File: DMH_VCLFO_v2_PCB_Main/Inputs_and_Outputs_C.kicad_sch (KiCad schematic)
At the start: 41 parts, among them J13 TS_Jack_6.35mm_Sw, J14 TS_Jack_6.35mm_Sw, J15 TS_Jack_6.35mm_Sw, J16 TS_Jack_6.35mm_Sw, J17 TS_Jack_6.35mm_Sw, J18 TS_Jack_6.35mm_Sw, J29 Conn_01x08, J30 Conn_01x08, J31 IDC_02x05, J32 Conn_01x08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

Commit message: Main PCB comp placement in progress
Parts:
- J13: Function CV In A -> CV In C
- J14: Function Sync A -> Sync C
- J15: Function Out A Sqr -> Out C Sqr
- J16: Function Out A Saw -> Out C Saw
- J17: Function Out A Rmp/Rnd -> Out C Rmp/Rnd
- J18: Function Out A Sin/Tri -> Out C Sin/Tri
- J29, J30: footprint Connector_PinHeader_2.54mm:PinHeader_1x08_P2.54mm_Vertical -> Connector_PinSocket_2.54mm:PinSocket_1x08_P2.54mm_Vertical
- RV10: Function Freq A -> Freq C
- RV9: Function CV A Amt -> CV C Amt
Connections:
- net Bus_CV_C: now also J30.5 (Pin_5), SW9.1 (A); no longer J30.8 (Pin_8), SW9.3 (C)
- net Bus_CV_M: now also J33.5 (Pin_5); no longer J33.8 (Pin_8)
- net C_BusCV_Sw_p2_C: now also J30.4 (Pin_4); no longer J30.7 (Pin_7)
- net C_BusCV_Sw_p2_M: now also J33.4 (Pin_4); no longer J33.7 (Pin_7)
- net C_CV_Amt_Pot_p2_C: now also J29.6 (Pin_6); no longer J29.4 (Pin_4)
- net C_CV_Amt_Pot_p2_M: now also J32.6 (Pin_6); no longer J32.4 (Pin_4)
- net C_FRng_Trim_p2_C: now also J29.1 (Pin_1); no longer J29.6 (Pin_6)
- net C_FRng_Trim_p2_M: now also J32.1 (Pin_1); no longer J32.6 (Pin_6)
- net C_Freq_Pot_p2_C: now also J29.4 (Pin_4); no longer J29.3 (Pin_3)
- net C_Freq_Pot_p2_M: now also J32.4 (Pin_4); no longer J32.3 (Pin_3)
- net C_Rmp_C: now also SW11.3 (C); no longer SW11.1 (A)
- net C_Rnd_C: now also SW11.1 (A); no longer SW11.3 (C)
- net C_Rng_Sw_p1_C: now also J29.3 (Pin_3); no longer J29.1 (Pin_1)
- net C_Rng_Sw_p1_M: now also J32.3 (Pin_3); no longer J32.1 (Pin_1)
- net C_Sin_C: now also J30.6 (Pin_6), SW12.3 (C); no longer J30.4 (Pin_4), SW12.1 (A)
- net C_Sin_M: now also J33.6 (Pin_6); no longer J33.4 (Pin_4)
- net C_Sin_Tri_Sw_p2_C: now also J30.7 (Pin_7); no longer J30.5 (Pin_5)
- net C_Sin_Tri_Sw_p2_M: now also J33.7 (Pin_7); no longer J33.5 (Pin_5)
- net C_Tri_C: now also J30.8 (Pin_8), SW12.1 (A); no longer J30.6 (Pin_6), SW12.3 (C)
- net C_Tri_M: now also J33.8 (Pin_8); no longer J33.6 (Pin_6)
- net C_VOct_Trim_p12_C: now also J29.8 (Pin_8); no longer J29.7 (Pin_7)
- net C_VOct_Trim_p12_M: now also J32.8 (Pin_8); no longer J32.7 (Pin_7)
- net C_VOct_Trim_p3_C: now also J29.7 (Pin_7); no longer J29.8 (Pin_8)
- net C_VOct_Trim_p3_M: now also J32.7 (Pin_7); no longer J32.8 (Pin_8)
- net Out A Rmp/Rnd TN renamed Out C Rmp/Rnd TN
- net Out A Saw TN renamed Out C Saw TN
- net Out A Sin/Tri TN renamed Out C Sin/Tri TN
- net Out A Sqr TN renamed Out C Sqr TN
- net Sync A TN renamed Sync C TN

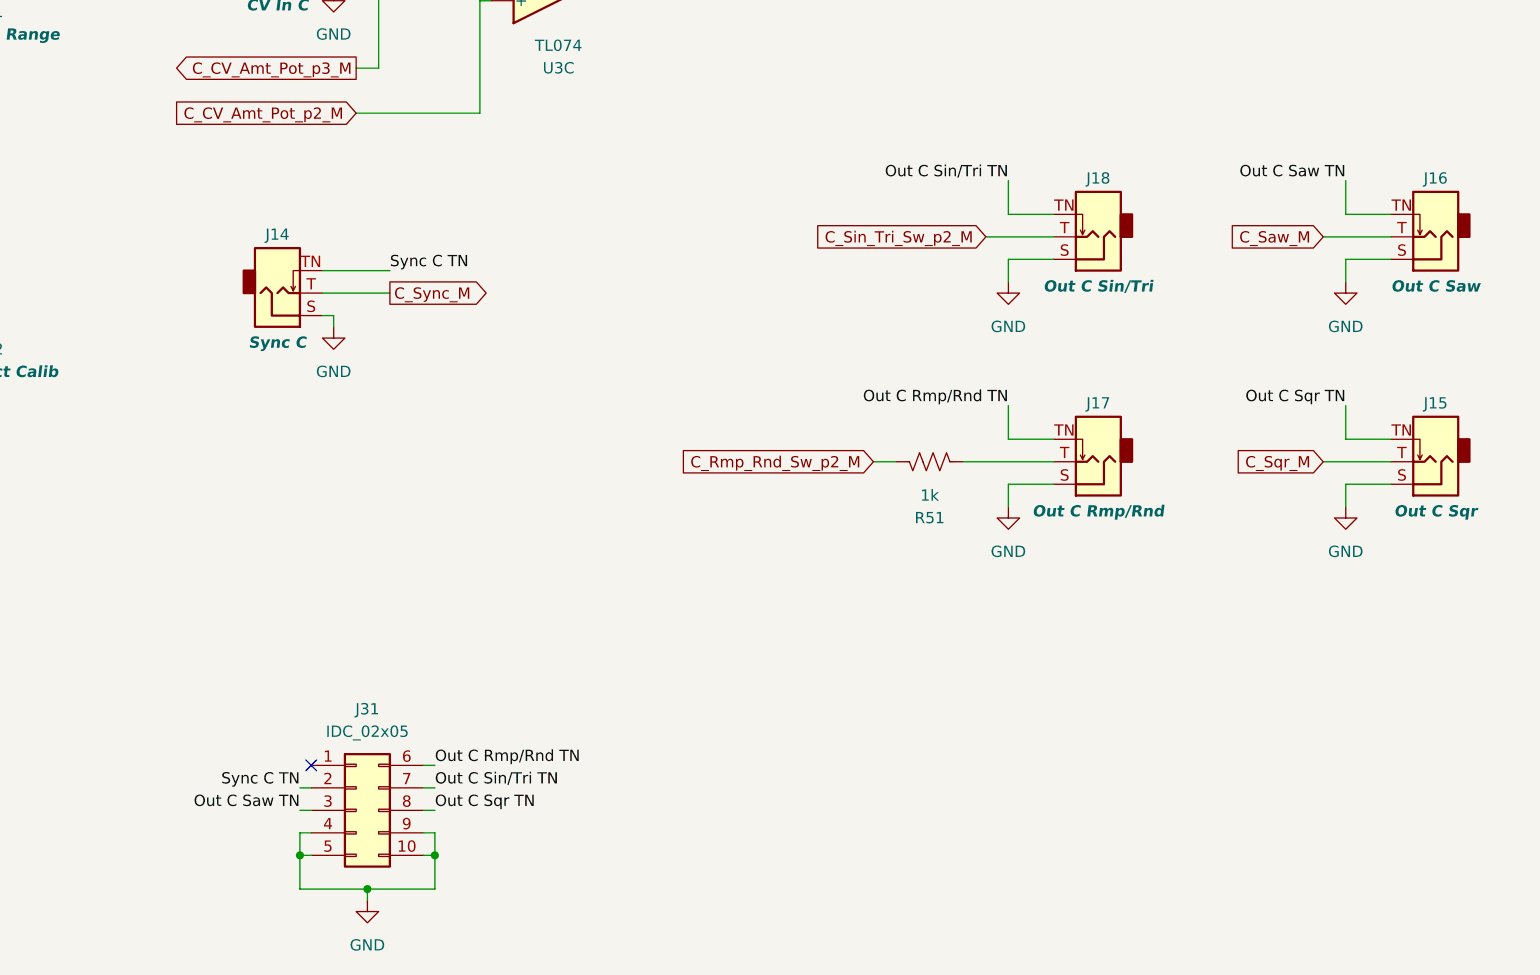
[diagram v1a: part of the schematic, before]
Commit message: Main PCB placement done
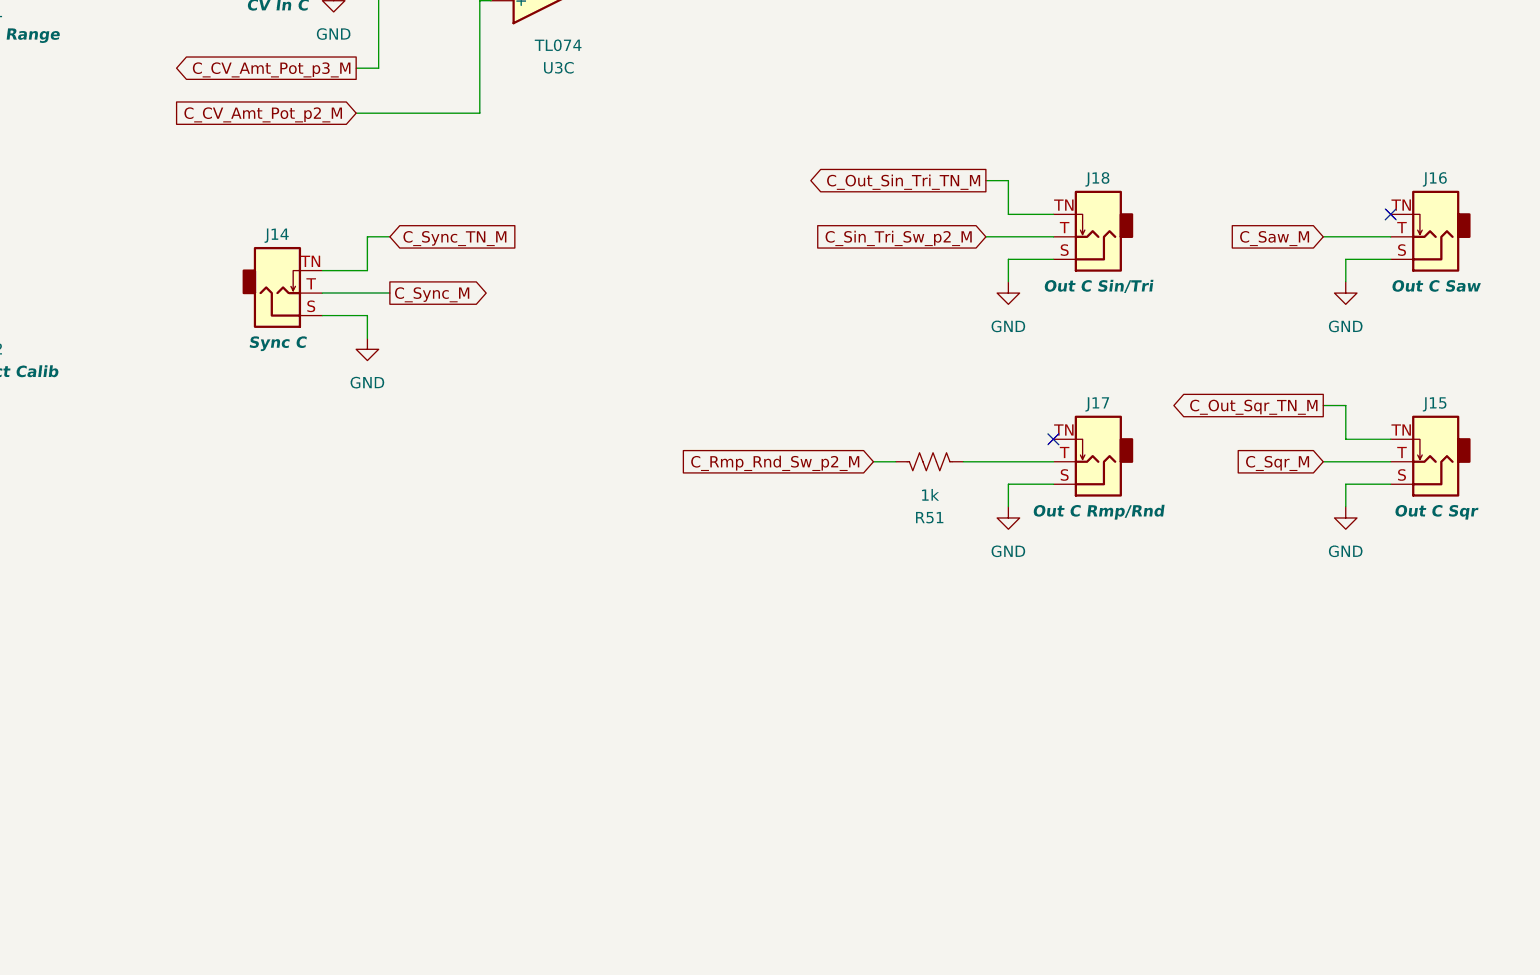
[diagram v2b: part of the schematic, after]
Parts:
- removed J31: IDC_02x05, SynthStuff:IDC-Header_2x05_P2.54mm_Vertical_BackBone, symbol SynthStuff:BackBone_Connector_10Pin
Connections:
- net Out C Rmp/Rnd TN: no longer names the net of J17.TN
- net Out C Saw TN: no longer names the net of J16.TN
- net Out C Sin/Tri TN renamed C_Out_Sin_Tri_TN_M
- net Out C Sqr TN renamed C_Out_Sqr_TN_M
- net Sync C TN renamed C_Sync_TN_M
- no-connect marks 2 -> 3

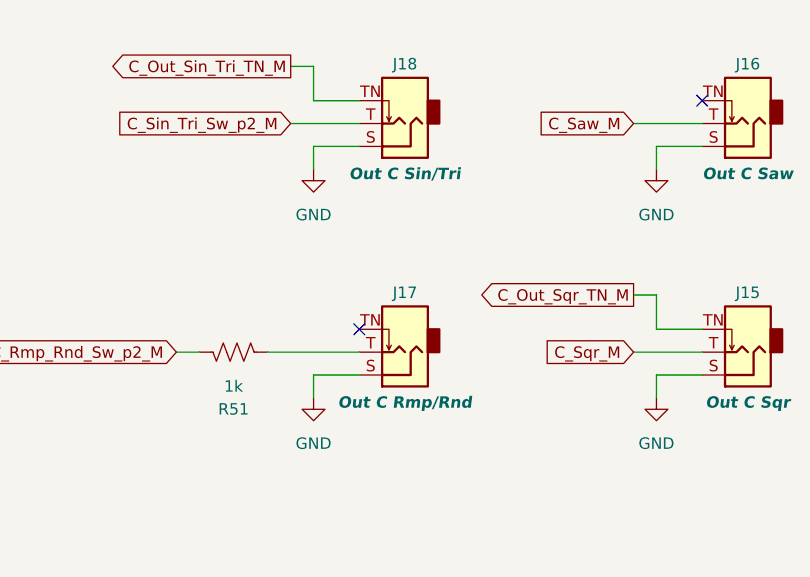
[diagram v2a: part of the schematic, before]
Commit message: Main PCB routing done
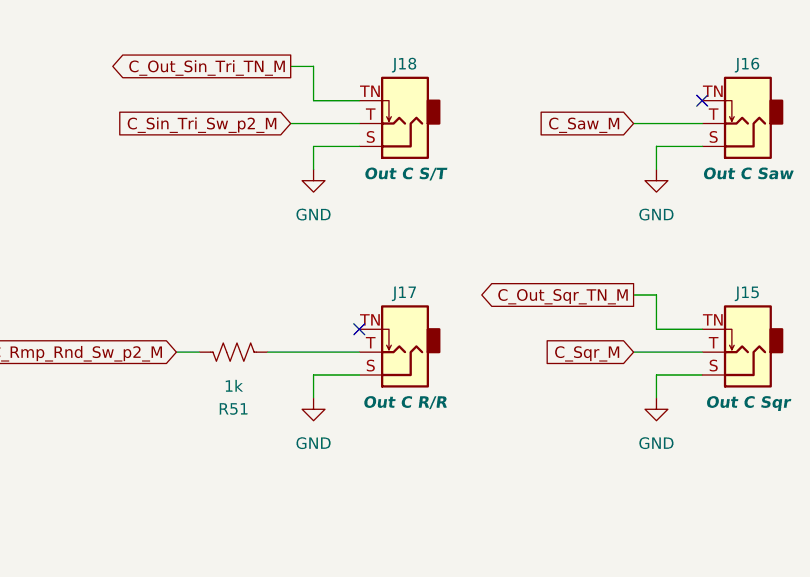
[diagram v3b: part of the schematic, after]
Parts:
- J17: Function Out C Rmp/Rnd -> Out C R/R
- J18: Function Out C Sin/Tri -> Out C S/T
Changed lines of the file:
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@@
 			)
 		)
-		(property "Function" "Out C Sin/Tri"
+		(property "Function" "Out C S/T"
 			(at 228.6 119.888 0)
 			(effects
@@
 			)
 		)
-		(property "Function" "Out C Rmp/Rnd"
+		(property "Function" "Out C R/R"
 			(at 228.6 145.288 0)
 			(effects

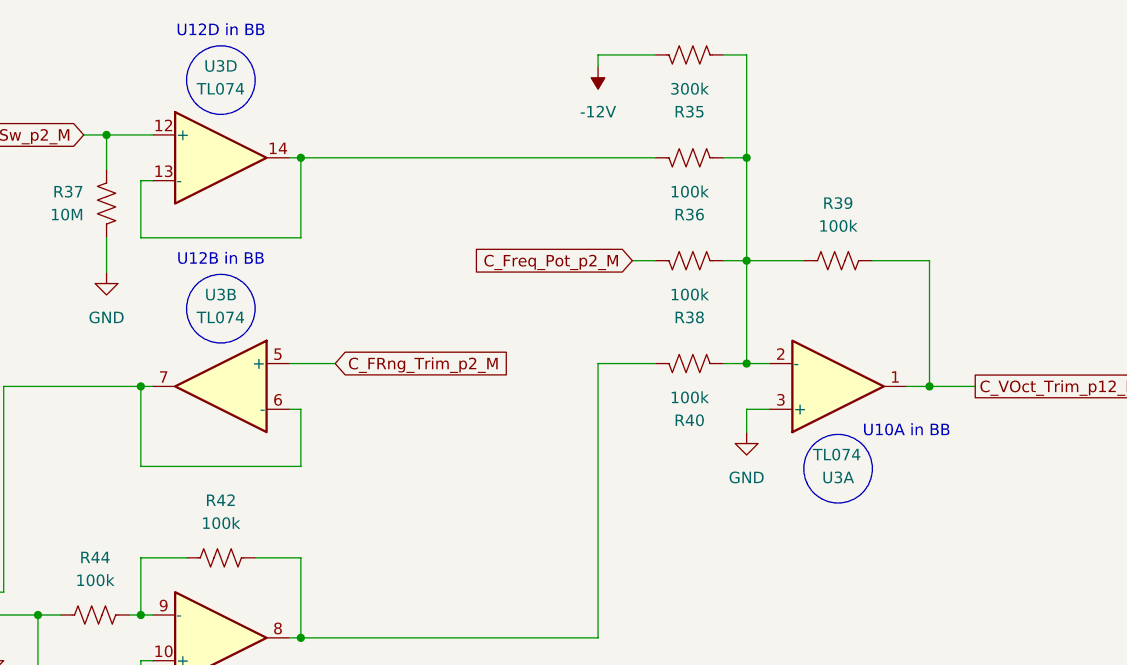
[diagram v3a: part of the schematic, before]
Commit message: Added project with Single VCLFO schematic
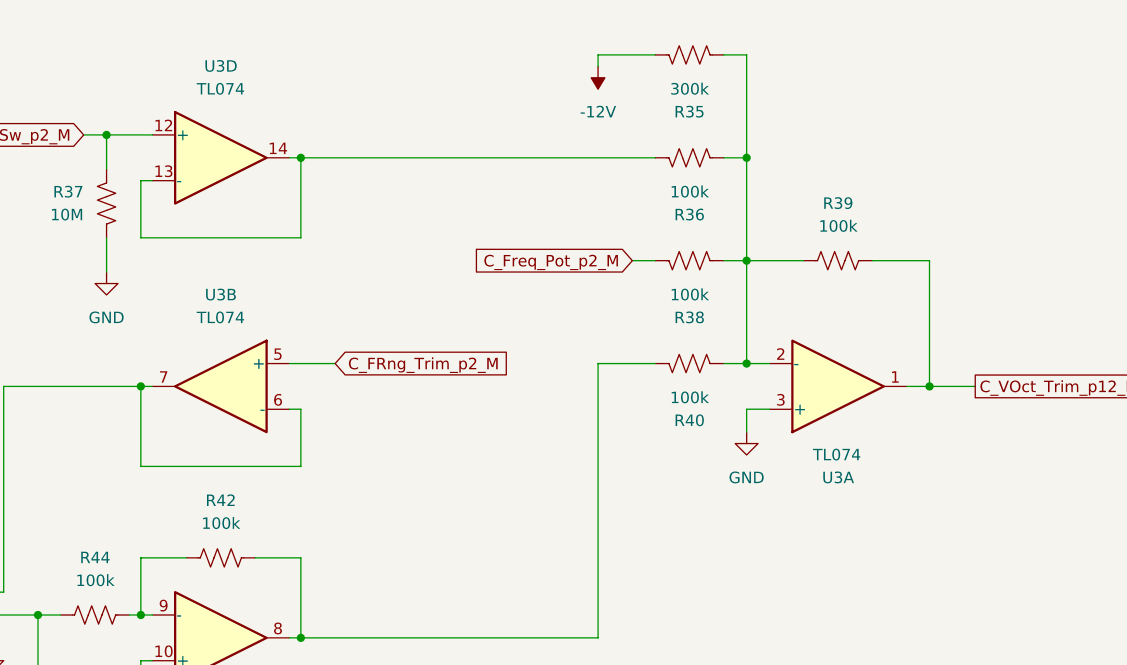
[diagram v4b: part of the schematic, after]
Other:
- note removed: "U10A in BB"
- note removed: "U12B in BB"
- note removed: "U12D in BB"
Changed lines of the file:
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@@
 		(comment 1 "PCB for 10cm Kosmo format synthesizer module")
-	)
-	(circle
-		(center 236.22 66.294)
-		(radius 3.81)
-		(stroke
-			(width 0)
-			(type default)
-		)
-		(fill
-			(type none)
-		)
-	)
-	(circle
-		(center 167.64 48.514)
-		(radius 3.81)
-		(stroke
-			(width 0)
-			(type default)
-		)
-		(fill
-			(type none)
-		)
-	)
-	(circle
-		(center 167.64 23.114)
-		(radius 3.81)
-		(stroke
-			(width 0)
-			(type default)
-		)
-		(fill
-			(type none)
-		)
-	)
-	(text "U12B in BB"
-		(exclude_from_sim no)
-		(at 167.64 43.18 0)
-		(effects
-			(font
-				(size 1.27 1.27)
-			)
-		)
-	)
-	(text "U10A in BB"
-		(exclude_from_sim no)
-		(at 243.84 62.23 0)
-		(effects
-			(font
-				(size 1.27 1.27)
-			)
-		)
-	)
-	(text "U12D in BB"
-		(exclude_from_sim no)
-		(at 167.64 17.78 0)
-		(effects
-			(font
-				(size 1.27 1.27)
-			)
-		)
 	)
 	(junction
